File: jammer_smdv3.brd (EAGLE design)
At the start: 51 parts, among them IC4 LM1458, Q2 MMBT3904

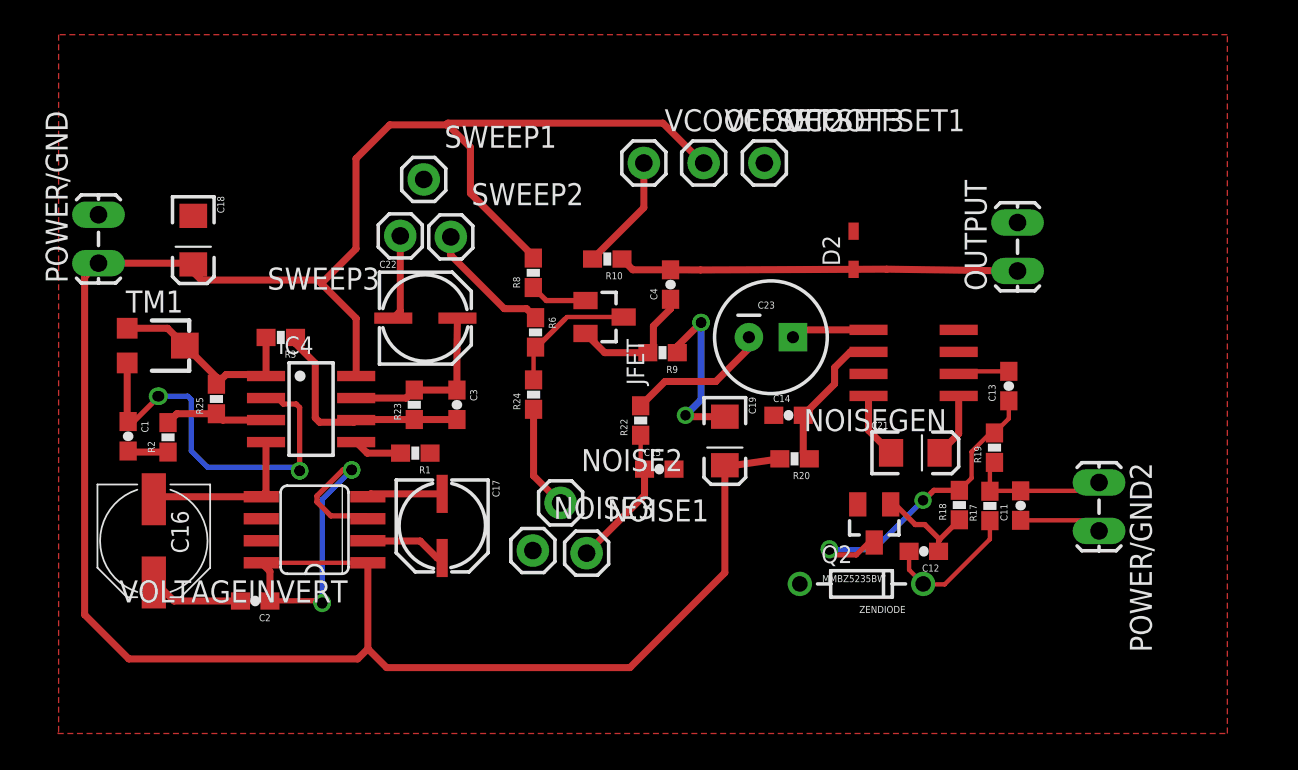
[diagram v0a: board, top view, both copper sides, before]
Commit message: updated github with rf board and vinyl stencil
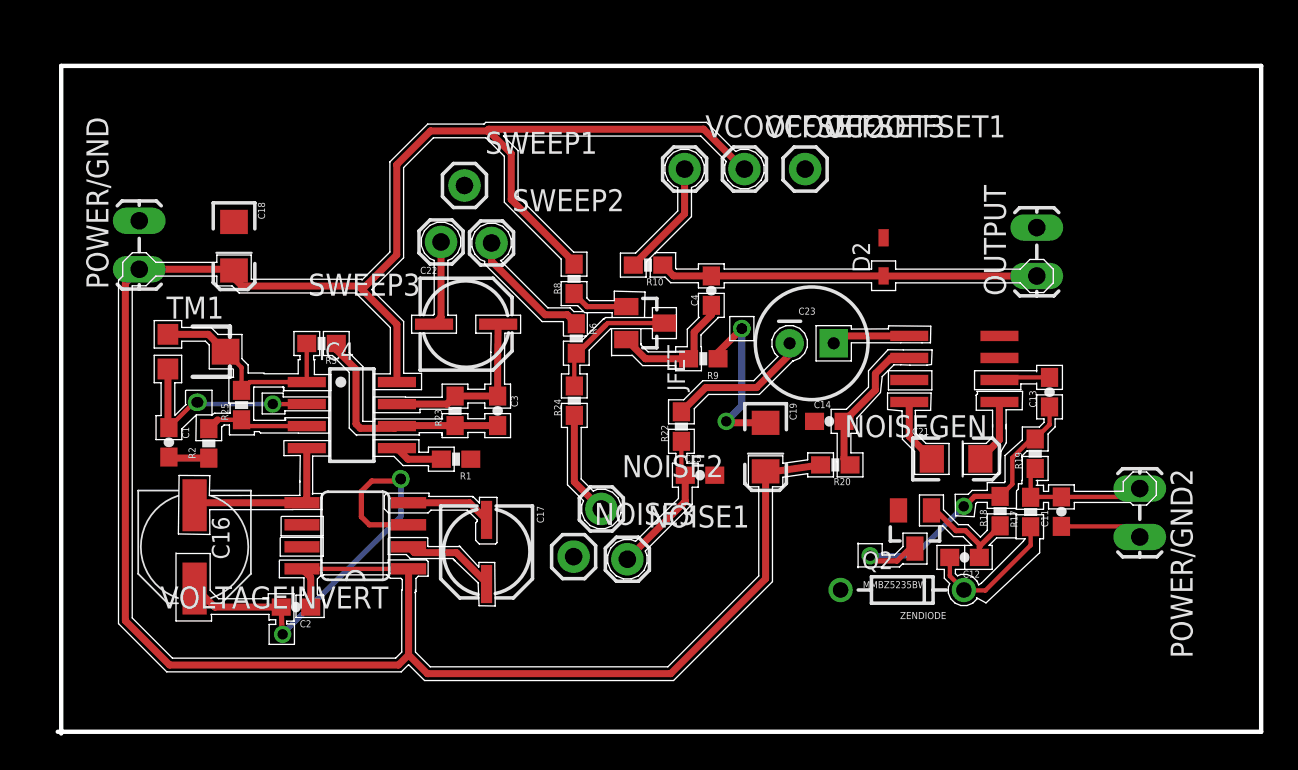
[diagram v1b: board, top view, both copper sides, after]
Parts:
- moved C17 2.97 mm to (24.8, 10.4)
- moved C11 2.38 mm to (57.8, 12.7)
- moved C12 2.38 mm to (52.2, 10.1)
- moved C19 2.38 mm to (40.7, 16.4)
- moved C21 2.38 mm to (51.7, 15.7)
- moved NOISE1 2.38 mm to (32.8, 9.95)
- moved NOISE2 2.38 mm to (31.2, 12.8)
- moved Q2 2.38 mm to (49.3, 11.7)
- moved R1 2.38 mm to (22.9, 15.7)
- moved R10 2.38 mm to (33.9, 26.9)
- moved R17 2.38 mm to (56.0, 12.7)
- moved R18 2.38 mm to (54.2, 12.7)
- moved R19 2.38 mm to (56.3, 16.0)
- moved R8 2.38 mm to (29.7, 26.1)
- moved SWEEP1 2.38 mm to (23.4, 31.5)
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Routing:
- net N$10: track 23.2 -> 12.0 mm
- net N$52: track 23.1 -> 21.8 mm
- net GND: track 42.4 -> 43.3 mm, vias 4 -> 3
- net N$4: track 4.70 -> 5.43 mm
- net N$5: track 4.35 -> 4.90 mm
- removed copper zone on layer 1, net GND
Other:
- board outline added: 69.4 x 38.5 mm
- board text added: "C1"
- board text added: "C11"
- board text added: "C12"
- board text added: "C13"
- board text added: "C14"
- board text added: "C15"
- board text added: "C16"
- board text added: "C17"
- board text added: "C18"
- board text added: "C19"
- board text added: "C2"
- board text added: "C21"
- board text added: "C22"
- board text added: "C23"
- board text added: "C3"
- board text added: "C4"
- board text added: "D2"
- board text added: "IC4"
- board text added: "JFET"
- board text added: "NOISE1"
- board text added: "NOISE2"
- board text added: "NOISE3"
- board text added: "NOISEGEN"
- board text added: "OUTPUT"
- board text added: "POWER/GND"
- board text added: "POWER/GND2"
- board text added: "Q2"
- board text added: "R1"
- board text added: "R10"
- board text added: "R17"
- board text added: "R18"
- board text added: "R19"
- board text added: "R2"
- board text added: "R20"
- board text added: "R22"
- board text added: "R23"
- board text added: "R24"
- board text added: "R3"
- board text added: "R6"
- board text added: "R8"
- board text added: "R9"
- board text added: "SWEEP1"
- board text added: "SWEEP2"
- board text added: "SWEEP3"
- board text added: "TM1"
- board text added: "VCOOFFSET1"
- board text added: "VCOOFFSET2"
- board text added: "VCOOFFSET3"
- board text added: "VOLTAGEINVERT"
- board text added: "ZENDIODE"
